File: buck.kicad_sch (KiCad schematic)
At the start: 35 parts, among them J7 Conn_01x02_Socket, Q3 BSC059N04LS6, Q4 BSC059N04LS6, U6 BQ24640

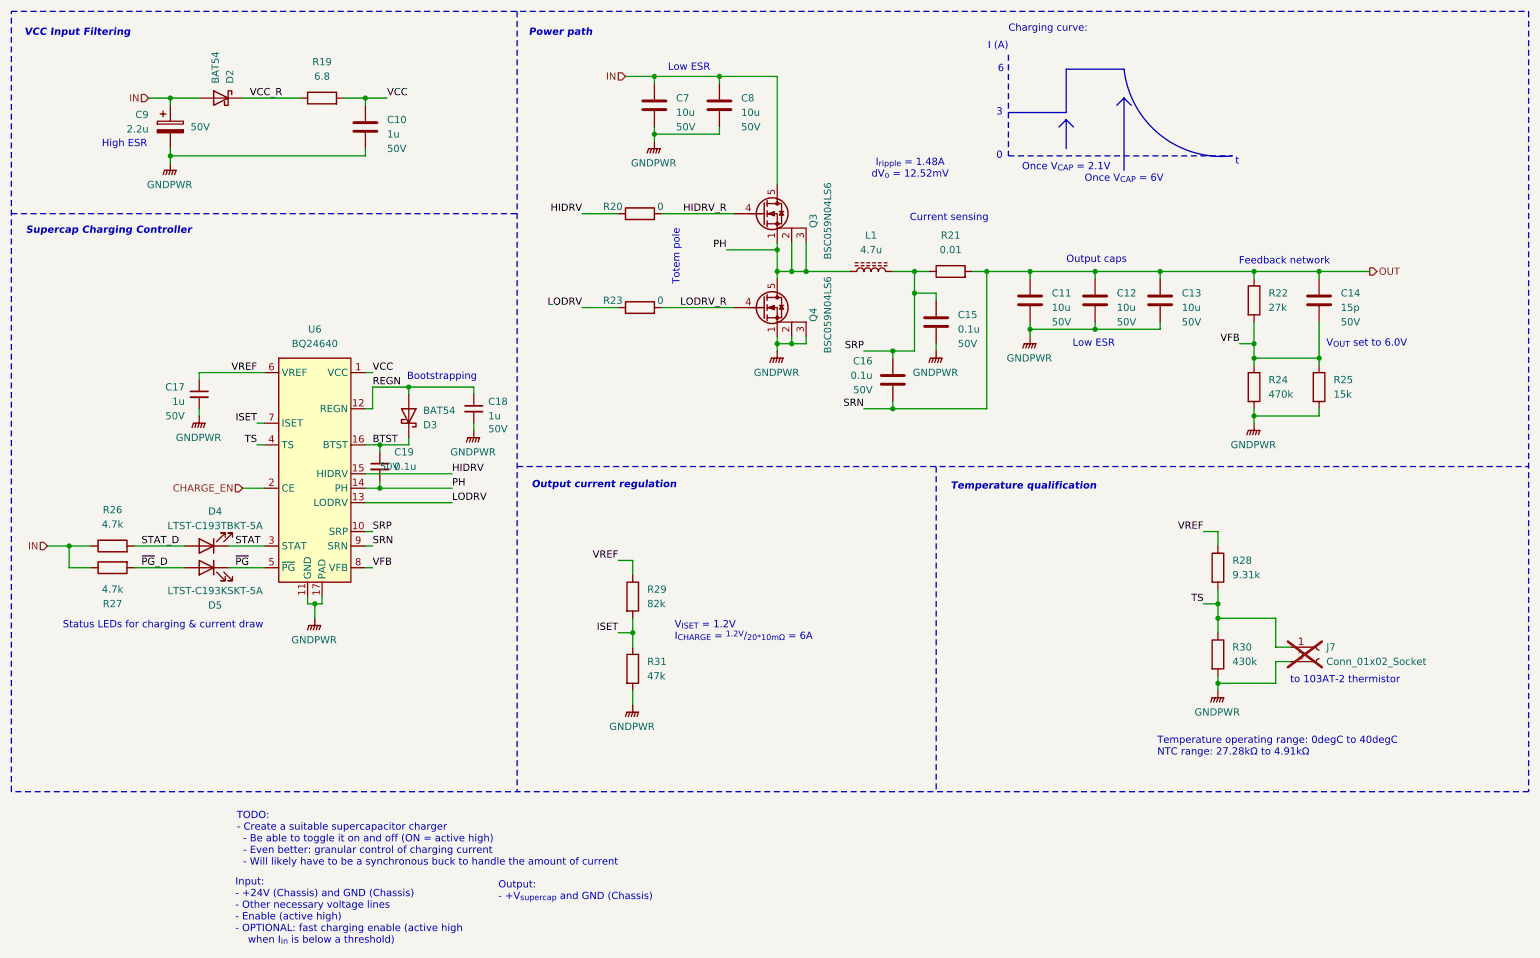
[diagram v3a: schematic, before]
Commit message: Add test points to all subsheets
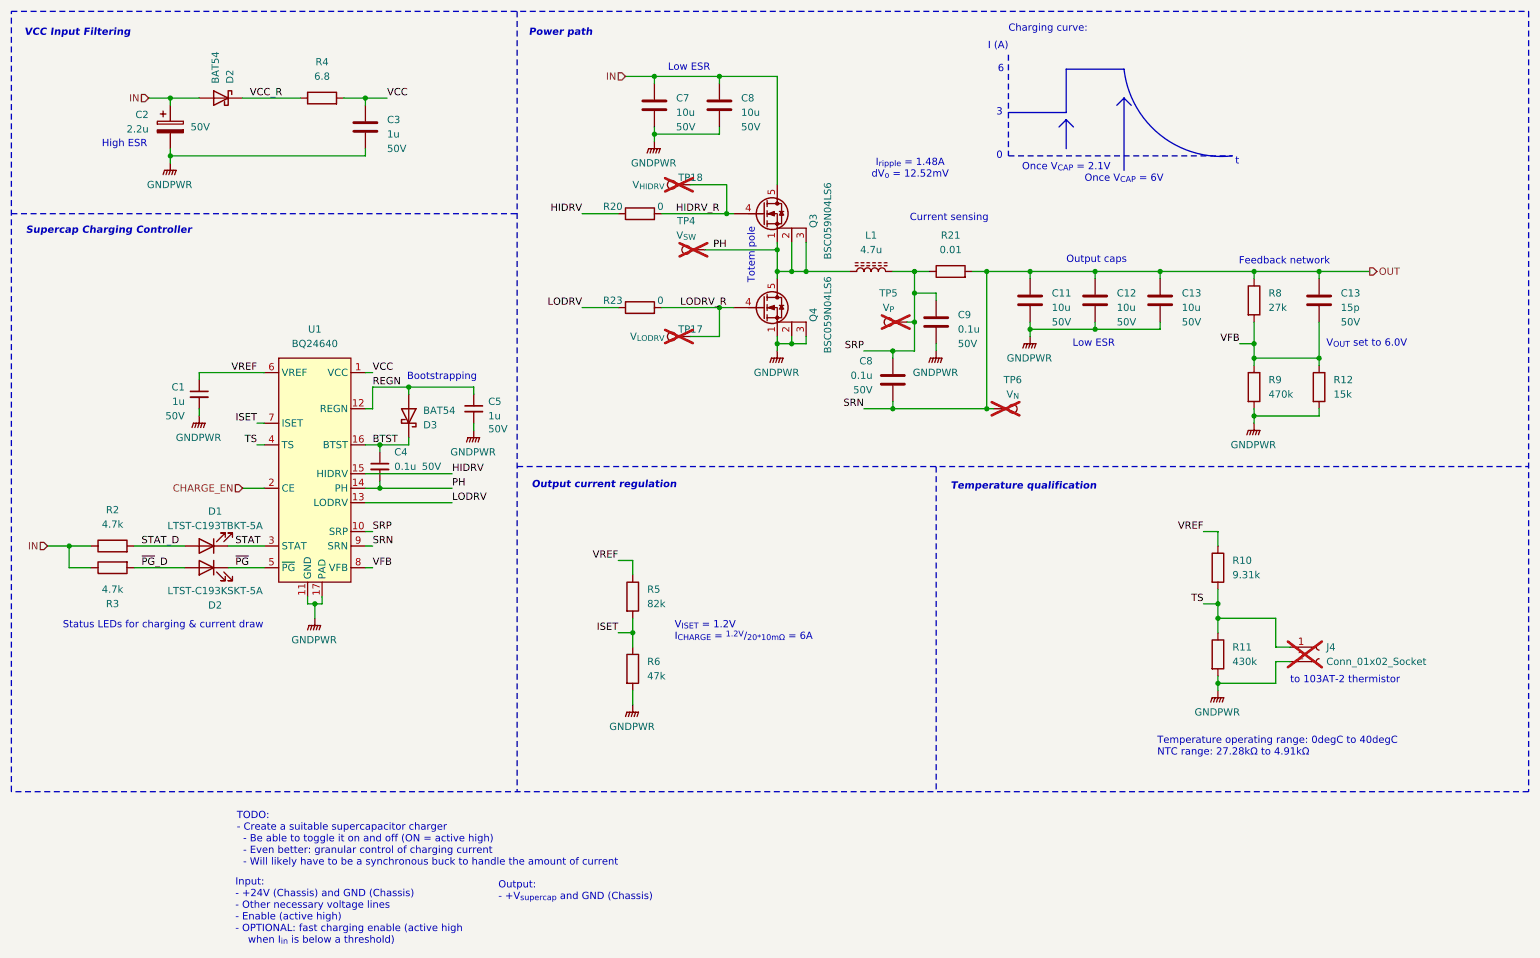
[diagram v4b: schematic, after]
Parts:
- added TP17: V_{LODRV}, TestPoint:TestPoint_Bridge_Pitch2.0mm_Drill0.7mm, symbol Connector:TestPoint
- added TP18: V_{HIDRV}, TestPoint:TestPoint_Bridge_Pitch2.0mm_Drill0.7mm, symbol Connector:TestPoint
- added TP4: V_{SW}, TestPoint:TestPoint_Bridge_Pitch2.0mm_Drill0.7mm, symbol Connector:TestPoint
- added TP5: V_{P}, TestPoint:TestPoint_Bridge_Pitch2.0mm_Drill0.7mm, symbol Connector:TestPoint
- added TP6: V_{N}, TestPoint:TestPoint_Bridge_Pitch2.0mm_Drill0.7mm, symbol Connector:TestPoint
- renumbered C17 to C1, C14 to C13, C9 to C2, C10 to C3, C19 to C4, C18 to C5, C16 to C8, C15 to C9, D4 to D1, D5 to D2, J7 to J4, R28 to R10, R30 to R11, R25 to R12, R26 to R2, R27 to R3, R19 to R4, R29 to R5, R31 to R6, R22 to R8, R24 to R9, U6 to U1
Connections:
- net HIDRV_R: now also TP18.1
- net LODRV_R: now also TP17.1
- net OUT: now also TP6.1
- net PH: now also TP4.1
- net SRP: now also TP5.1

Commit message: Renumbered components for rev 1b layout
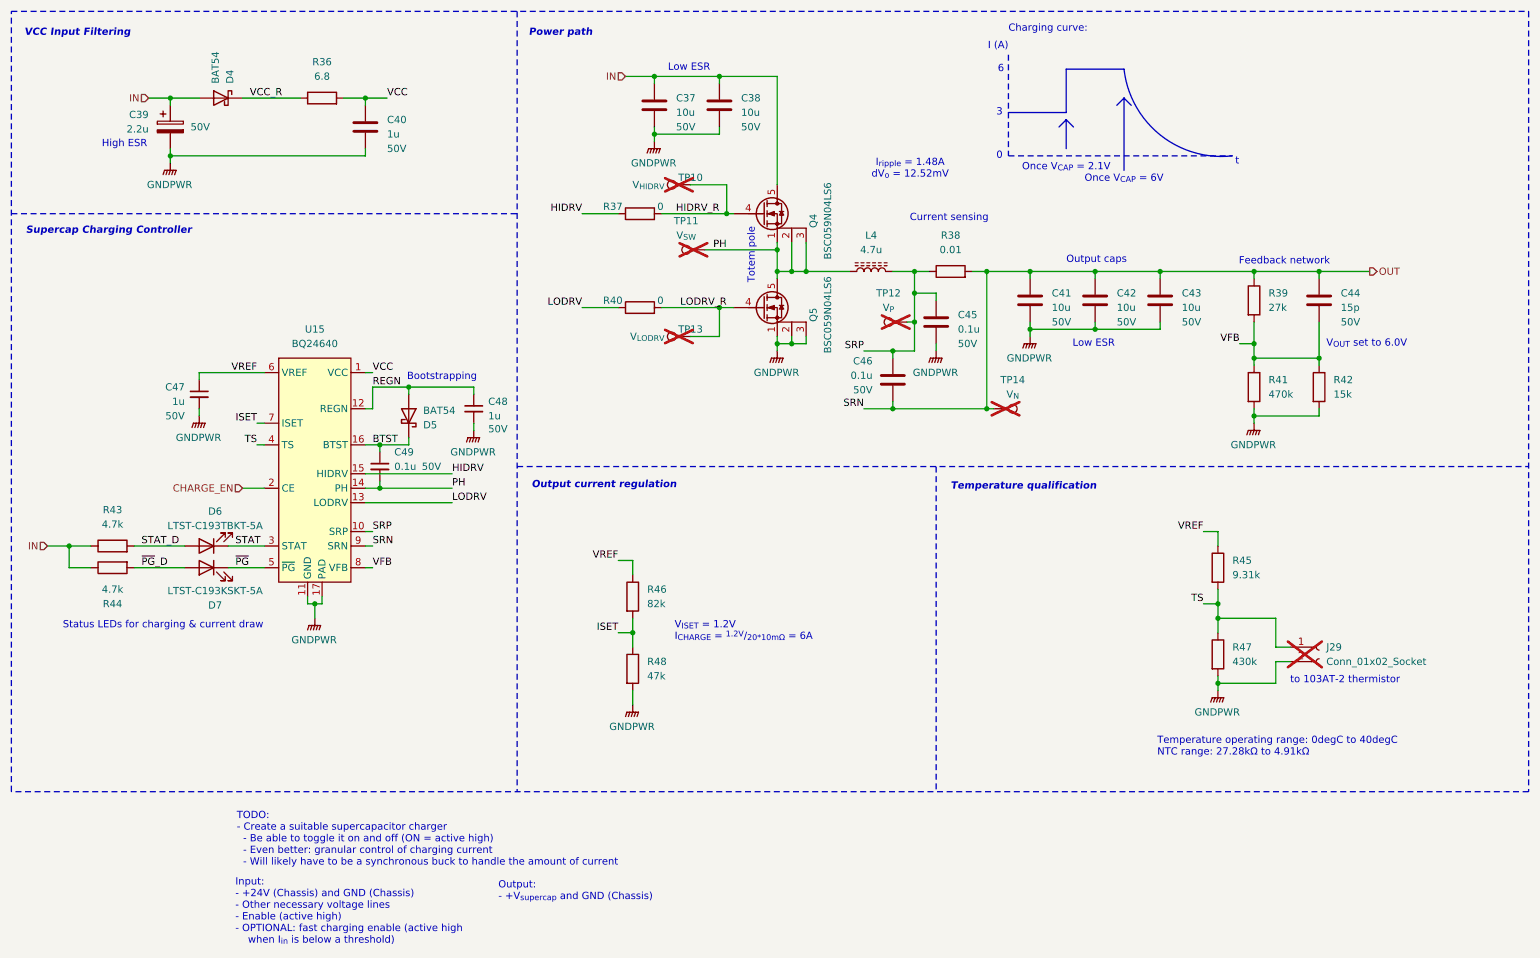
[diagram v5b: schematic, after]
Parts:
- renumbered C7 to C37, C8 to C38, C2 to C39, C3 to C40, C11 to C41, C12 to C42, C13 to C43, C13 to C44, C9 to C45, C8 to C46, C1 to C47, C5 to C48, C4 to C49, D2 to D4, D3 to D5, D1 to D6, D2 to D7, J4 to J29, L1 to L4, Q3 to Q4, Q4 to Q5, R4 to R36, R20 to R37, R21 to R38, R8 to R39, R23 to R40, R9 to R41, R12 to R42, R2 to R43, R3 to R44, R10 to R45, R5 to R46, R11 to R47, R6 to R48, TP18 to TP10, TP4 to TP11, TP5 to TP12, TP17 to TP13, TP6 to TP14, U1 to U15

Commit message: Begin layout
Completed ideal diode layout
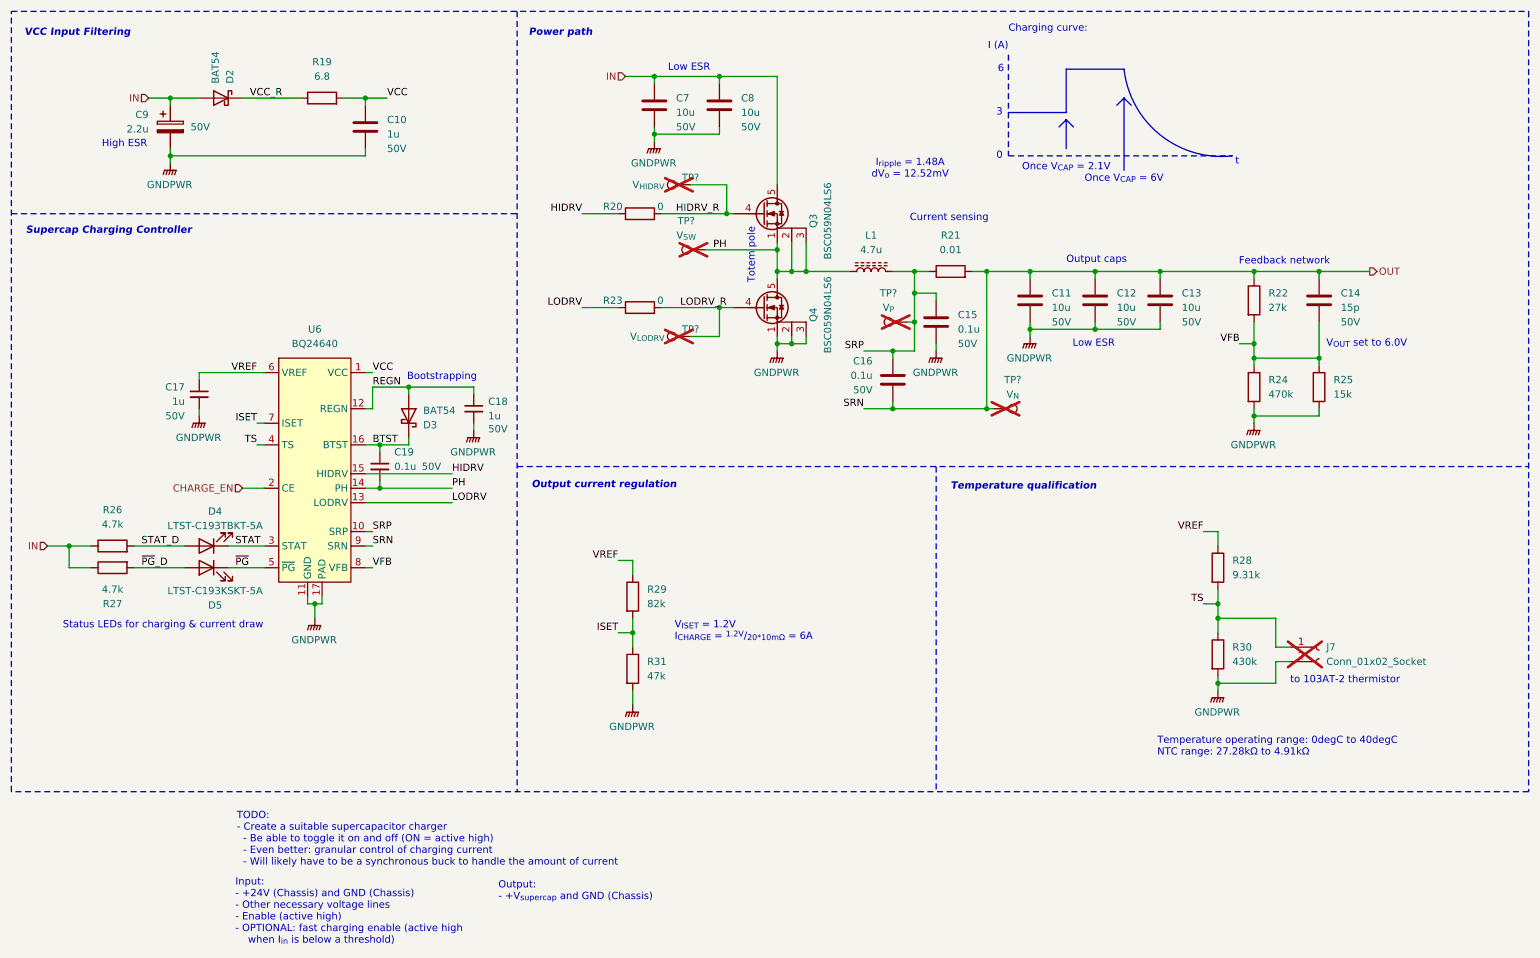
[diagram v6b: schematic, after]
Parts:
- renumbered C40 to C10, C41 to C11, C42 to C12, C43 to C13, C44 to C14, C45 to C15, C46 to C16, C47 to C17, C48 to C18, C49 to C19, C37 to C7, C38 to C8, C39 to C9, D4 to D2, D5 to D3, D6 to D4, D7 to D5, J29 to J7, L4 to L1, Q4 to Q3, Q5 to Q4, R36 to R19, R37 to R20, R38 to R21, R39 to R22, R40 to R23, R41 to R24, R42 to R25, R43 to R26, R44 to R27, R45 to R28, R46 to R29, R47 to R30, R48 to R31, TP13 to TP?, TP14 to TP?, TP10 to TP?, TP11 to TP?, TP12 to TP?, U15 to U6
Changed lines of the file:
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@@
 		(on_board yes)
 		(dnp no)
-		(property "Reference" "D5"
+		(property "Reference" "D3"
 			(at 86.36 96.8376 90)
 			(effects
@@
 		(dnp no)
 		(fields_autoplaced yes)
-		(property "Reference" "R39"
+		(property "Reference" "R22"
 			(at 234.95 73.6599 0)
 			(effects
@@
 		(dnp no)
 		(fields_autoplaced yes)
-		(property "Reference" "#PWR098"
+		(property "Reference" "#PWR037"
 			(at 193.04 86.36 0)
 			(effects
@@
 		(on_board yes)
 		(dnp no)
-		(property "Reference" "C42"
+		(property "Reference" "C12"
 			(at 208.28 73.6599 0)
 			(effects
@@
 		(on_board yes)
 		(dnp no)
-		(property "Reference" "Q4"
+		(property "Reference" "Q3"
 			(at 154.94 60.96 90)
 			(effects
@@
 		(dnp no)
 		(fields_autoplaced yes)
-		(property "Reference" "R47"
+		(property "Reference" "R30"
 			(at 228.6 135.8899 0)
 			(effects
@@
 		(dnp no)
 		(fields_autoplaced yes)
-		(property "Reference" "#PWR0103"
+		(property "Reference" "#PWR042"
 			(at 95.25 102.87 0)
 			(effects
@@
 		(on_board yes)
 		(dnp no)
-		(property "Reference" "D7"
+		(property "Reference" "D5"
 			(at 49.784 128.524 0)
 			(effects
@@
 		(dnp no)
 		(fields_autoplaced yes)
-		(property "Reference" "#PWR0106"
+		(property "Reference" "#PWR045"
 			(at 123.19 151.13 0)
 			(effects
@@
 		(dnp no)
 		(fields_autoplaced yes)
-		(property "Reference" "U15"
+		(property "Reference" "U6"
 			(at 67.31 80.01 0)
 			(effects
@@
 		(dnp no)
 		(fields_autoplaced yes)
-		(property "Reference" "#PWR0105"
+		(property "Reference" "#PWR044"
 			(at 226.06 148.59 0)
 			(effects
@@
 		(on_board yes)
 		(dnp no)
-		(property "Reference" "R37"
+		(property "Reference" "R20"
 			(at 121.412 59.182 90)
 			(effects
@@
 		(on_board yes)
 		(dnp no)
-		(property "Reference" "C43"
+		(property "Reference" "C13"
 			(at 219.71 73.6599 0)
 			(effects
@@
 		(dnp no)
 		(fields_autoplaced yes)
-		(property "Reference" "R36"
+		(property "Reference" "R19"
 			(at 68.58 33.02 90)
 			(effects
@@
 		(on_board yes)
 		(dnp no)
-		(property "Reference" "R44"
+		(property "Reference" "R27"
 			(at 31.75 128.27 90)
 			(effects
@@
 		(on_board yes)
 		(dnp no)
-		(property "Reference" "C48"
+		(property "Reference" "C18"
 			(at 97.79 92.7162 0)
 			(effects
@@
 		(on_board yes)
 		(dnp no)
-		(property "Reference" "D4"
+		(property "Reference" "D2"
 			(at 52.3876 36.83 90)
 			(effects
@@
 		(dnp no)
 		(fields_autoplaced yes)
-		(property "Reference" "R42"
+		(property "Reference" "R25"
 			(at 246.38 88.8999 0)
 			(effects
@@
 		(dnp no)
 		(fields_autoplaced yes)
-		(property "Reference" "#PWR0104"
+		(property "Reference" "#PWR043"
 			(at 67.31 135.89 0)
 			(effects
@@
 		(on_board yes)
 		(dnp no)
-		(property "Reference" "Q5"
+		(property "Reference" "Q4"
 			(at 154.94 77.47 90)
 			(effects
@@
 		(on_board yes)
 		(dnp no)
-		(property "Reference" "C39"
+		(property "Reference" "C9"
 			(at 38.1 42.2909 0)
 			(effects
@@
 		(on_board yes)
 		(dnp no)
-		(property "Reference" "D6"
+		(property "Reference" "D4"
 			(at 49.784 112.014 0)
 			(effects
@@
 		(on_board yes)
 		(dnp no)
-		(property "Reference" "C41"
+		(property "Reference" "C11"
 			(at 196.85 73.6599 0)
 			(effects
@@
 		(on_board yes)
 		(dnp no)
-		(property "Reference" "R40"
+		(property "Reference" "R23"
 			(at 121.412 75.692 90)
 			(effects
@@
 		(dnp yes)
 		(fields_autoplaced yes)
-		(property "Reference" "J29"
+		(property "Reference" "J7"
 			(at 245.11 135.8899 0)
 			(effects
@@
 		(on_board yes)
 		(dnp no)
-		(property "Reference" "C47"
+		(property "Reference" "C17"
 			(at 44.45 90.1762 0)
 			(effects
@@
 		(dnp no)
 		(fields_autoplaced yes)
-		(property "Reference" "R48"
+		(property "Reference" "R31"
 			(at 125.73 138.4299 0)
 			(effects
@@
 		(dnp no)
 		(fields_autoplaced yes)
-		(property "Reference" "R45"
+		(property "Reference" "R28"
 			(at 228.6 120.6499 0)
 			(effects
@@
 		(dnp no)
 		(fields_autoplaced yes)
-		(property "Reference" "R46"
+		(property "Reference" "R29"
 			(at 125.73 125.7299 0)
 			(effects
@@
 		(dnp no)
 		(fields_autoplaced yes)
-		(property "Reference" "#PWR0101"
+		(property "Reference" "#PWR040"
 			(at 46.99 100.33 0)
 			(effects
@@
 		(dnp no)
 		(fields_autoplaced yes)
-		(property "Reference" "L4"
+		(property "Reference" "L1"
 			(at 165.1 63.5 90)
 			(effects
@@
 		(dnp no)
 		(fields_autoplaced yes)
-		(property "Reference" "R38"
+		(property "Reference" "R21"
 			(at 179.07 63.5 90)
 			(effects
@@
 		(dnp no)
 		(fields_autoplaced yes)
-		(property "Reference" "#PWR0102"
+		(property "Reference" "#PWR041"
 			(at 232.41 101.6 0)
 			(effects
@@
 		(on_board yes)
 		(dnp yes)
-		(property "Reference" "TP13"
+		(property "Reference" "TP?"
 			(at 133.35 80.01 90)
 			(effects
@@
 		)
 		(instances
+			(project "SupercapManager"
+				(path "/6197145b-e7d4-44cc-9d90-537b6501bf60/388608c4-ca49-4b14-9684-8f150e280879"
+					(reference "TP?")
+					(unit 1)
+				)
+			)
 			(project "Rev 1B"
 				(path "/e5f99deb-ef42-4c5f-b80a-388477910e20/74b869e2-2f46-4217-991e-e066eaeda764"
@@
 		(on_board yes)
 		(dnp no)
-		(property "Reference" "C46"
+		(property "Reference" "C16"
 			(at 165.354 85.598 0)
 			(effects
@@
 		(on_board yes)
 		(dnp no)
-		(property "Reference" "C45"
+		(property "Reference" "C15"
 			(at 180.34 77.4699 0)
 			(effects
@@
 		(dnp no)
 		(fields_autoplaced yes)
-		(property "Reference" "R41"
+		(property "Reference" "R24"
 			(at 234.95 88.8999 0)
 			(effects
@@
 		(on_board yes)
 		(dnp yes)
-		(property "Reference" "TP14"
+		(property "Reference" "TP?"
 			(at 189.992 88.9 90)
 			(effects
@@
 		)
 		(instances
+			(project "SupercapManager"
+				(path "/6197145b-e7d4-44cc-9d90-537b6501bf60/388608c4-ca49-4b14-9684-8f150e280879"
+					(reference "TP?")
+					(unit 1)
+				)
+			)
 			(project "Rev 1B"
 				(path "/e5f99deb-ef42-4c5f-b80a-388477910e20/74b869e2-2f46-4217-991e-e066eaeda764"
@@
 		(on_board yes)
 		(dnp yes)
-		(property "Reference" "TP10"
+		(property "Reference" "TP?"
 			(at 133.35 53.34 90)
 			(effects
@@
 		)
 		(instances
+			(project "SupercapManager"
+				(path "/6197145b-e7d4-44cc-9d90-537b6501bf60/388608c4-ca49-4b14-9684-8f150e280879"
+					(reference "TP?")
+					(unit 1)
+				)
+			)
 			(project "Rev 1B"
 				(path "/e5f99deb-ef42-4c5f-b80a-388477910e20/74b869e2-2f46-4217-991e-e066eaeda764"
@@
 		(on_board yes)
 		(dnp no)
-		(property "Reference" "C38"
+		(property "Reference" "C8"
 			(at 142.24 39.3699 0)
 			(effects
@@
 		(dnp no)
 		(fields_autoplaced yes)
-		(property "Reference" "R43"
+		(property "Reference" "R26"
 			(at 31.75 111.76 90)
 			(effects
@@
 		(dnp no)
 		(fields_autoplaced yes)
-		(property "Reference" "#PWR096"
+		(property "Reference" "#PWR035"
 			(at 127 52.07 0)
 			(effects
@@
 		(on_board yes)
 		(dnp no)
-		(property "Reference" "C44"
+		(property "Reference" "C14"
 			(at 247.65 73.6599 0)
 			(effects
@@
 		(dnp no)
 		(fields_autoplaced yes)
-		(property "Reference" "#PWR097"
+		(property "Reference" "#PWR036"
 			(at 41.91 55.88 0)
 			(effects
@@
 		(dnp no)
 		(fields_autoplaced yes)
-		(property "Reference" "#PWR0100"
+		(property "Reference" "#PWR039"
 			(at 176.53 88.9 0)
 			(effects
@@
 		(dnp no)
 		(fields_autoplaced yes)
-		(property "Reference" "#PWR099"
+		(property "Reference" "#PWR038"
 			(at 148.59 88.9 0)
 			(effects
@@
 		(on_board yes)
 		(dnp no)
-		(property "Reference" "C49"
+		(property "Reference" "C19"
 			(at 81.28 101.6 0)
 			(effects
@@
 		(on_board yes)
 		(dnp no)
-		(property "Reference" "C40"
+		(property "Reference" "C10"
 			(at 80.01 43.1799 0)
 			(effects
@@
 		(dnp yes)
 		(fields_autoplaced yes)
-		(property "Reference" "TP11"
+		(property "Reference" "TP?"
 			(at 132.588 60.96 90)
 			(effects
@@
 		)
 		(instances
+			(project "SupercapManager"
+				(path "/6197145b-e7d4-44cc-9d90-537b6501bf60/388608c4-ca49-4b14-9684-8f150e280879"
+					(reference "TP?")
+					(unit 1)
+				)
+			)
 			(project "Rev 1B"
 				(path "/e5f99deb-ef42-4c5f-b80a-388477910e20/74b869e2-2f46-4217-991e-e066eaeda764"
@@
 		(dnp yes)
 		(fields_autoplaced yes)
-		(property "Reference" "TP12"
+		(property "Reference" "TP?"
 			(at 168.148 73.66 90)
 			(effects
@@
 		)
 		(instances
+			(project "SupercapManager"
+				(path "/6197145b-e7d4-44cc-9d90-537b6501bf60/388608c4-ca49-4b14-9684-8f150e280879"
+					(reference "TP?")
+					(unit 1)
+				)
+			)
 			(project "Rev 1B"
 				(path "/e5f99deb-ef42-4c5f-b80a-388477910e20/74b869e2-2f46-4217-991e-e066eaeda764"
@@
 		(on_board yes)
 		(dnp no)
-		(property "Reference" "C37"
+		(property "Reference" "C7"
 			(at 130.81 39.3699 0)
 			(effects
